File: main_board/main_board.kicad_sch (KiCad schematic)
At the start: 85 parts, among them J2 Conn_01x02, J3 Conn_01x02, J4 EncSide, J5 MainSide, J6 EncSide, J7 MainSide, Q1 ST-1KL3A, Q2 ST-1KL3A, Q3 ST-1KL3A, Q4 ST-1KL3A, Q5 IRLML6344, Q6 IRLML6344, Q7 IRLML6344, Q8 IRLML6344, U1 ADCS7476, U10 AS5047D, U11 LSM6DSR, U2 BD63573NUV, U3 ADCS7476, U4 ADCS7476, U5 BD63573NUV, U6 ESP32-S3-PICO-1-N8R2, U7 AS5047D, U8 ADCS7476, U9 ADCS7476

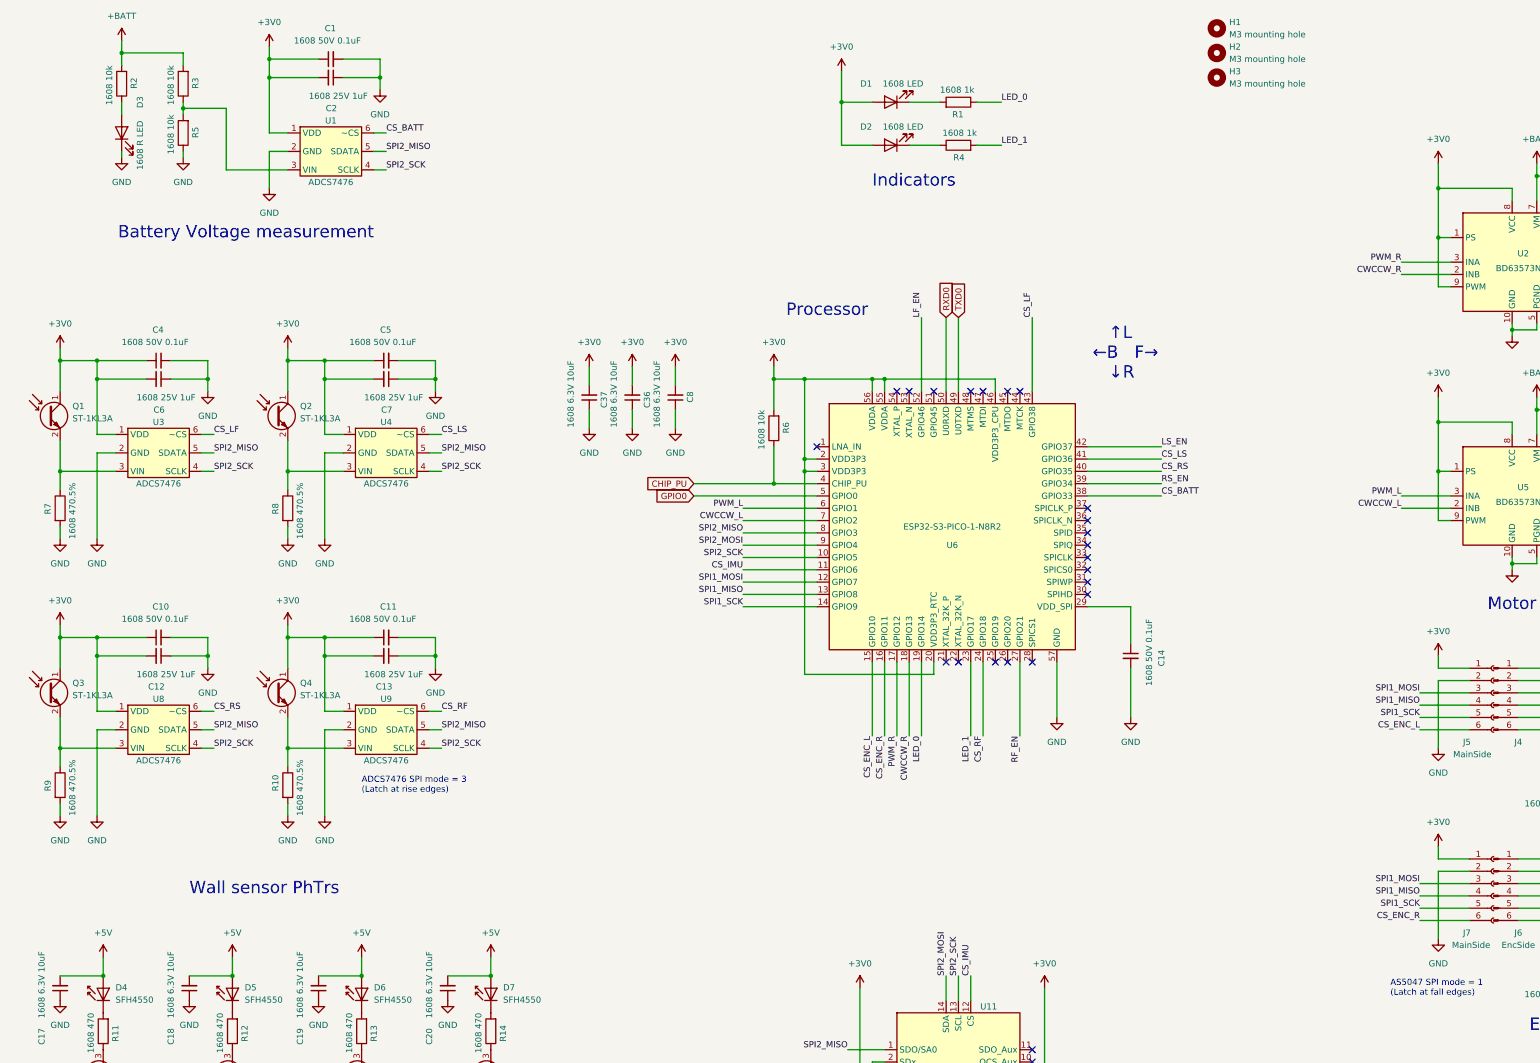
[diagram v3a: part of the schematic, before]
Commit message: 回路図 : 3.0Vから3.3Vに変更 アートワーク : コネクタピン配などのシルクを追加
Signed-off-by: Kazuki Iida <elkel53930@gmail.com>
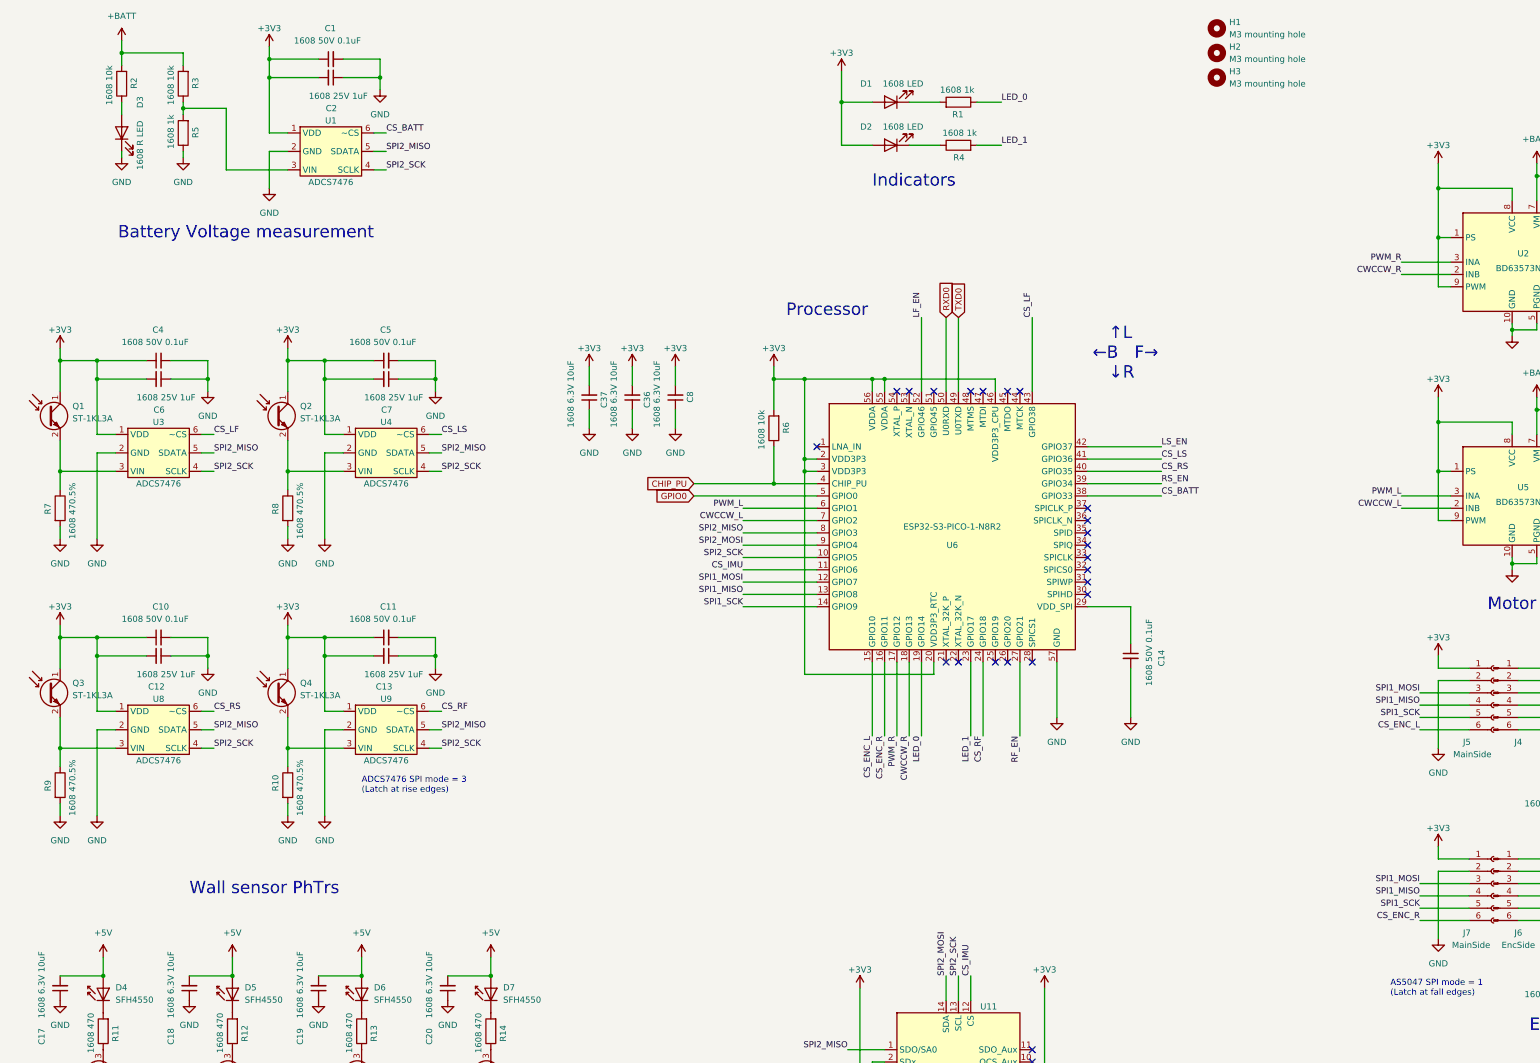
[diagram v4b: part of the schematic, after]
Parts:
- R5: value 1608 10k -> 1608 1k
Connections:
- net +3V0 renamed +3V3

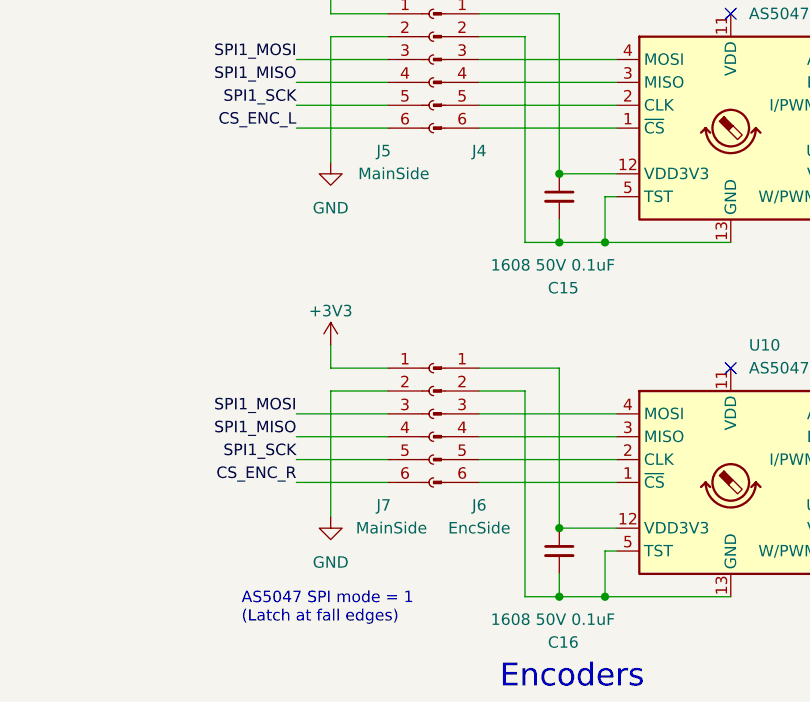
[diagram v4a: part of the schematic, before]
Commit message: 定数や型番の修正
Signed-off-by: Kazuki Iida <elkel53930@gmail.com>
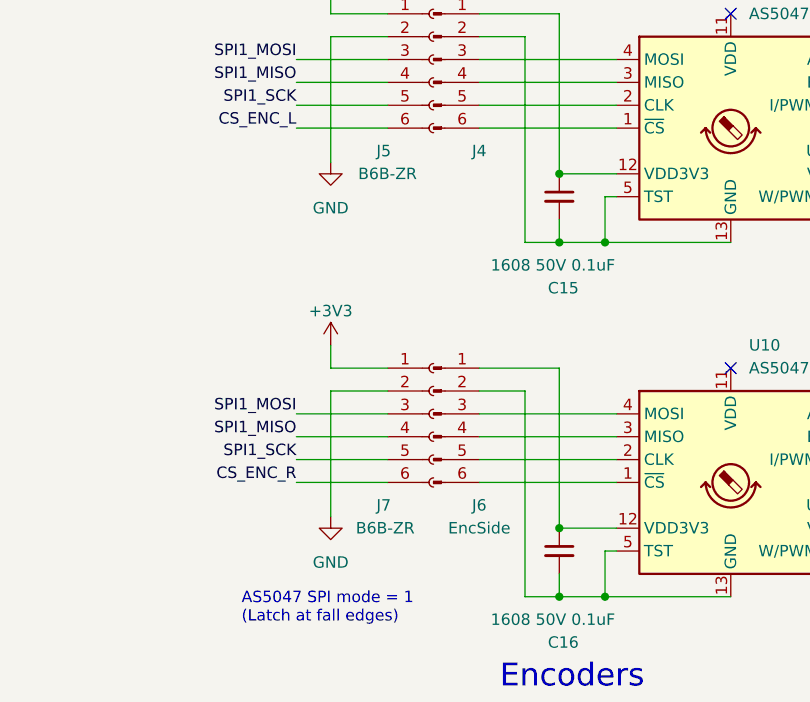
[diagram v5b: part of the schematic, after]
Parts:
- J5, J7: value MainSide -> B6B-ZR
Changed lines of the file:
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@@
 			)
 		)
-		(property "Value" "MainSide"
+		(property "Value" "B6B-ZR"
 			(at 325.374 213.36 0)
 			(effects
@@
 			)
 		)
-		(property "Value" "MainSide"
+		(property "Value" "B6B-ZR"
 			(at 325.628 173.99 0)
 			(effects

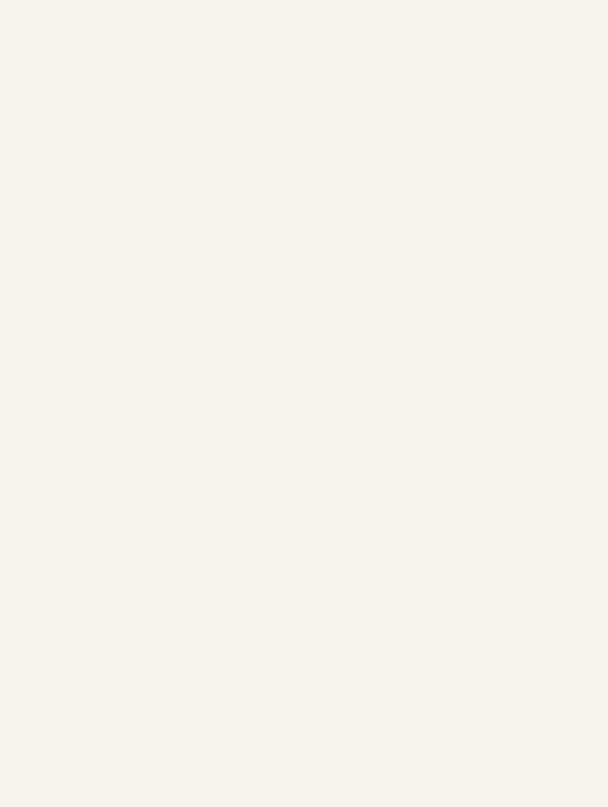
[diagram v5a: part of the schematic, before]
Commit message: 充電回路追加
Signed-off-by: Kazuki Iida <elkel53930@gmail.com>
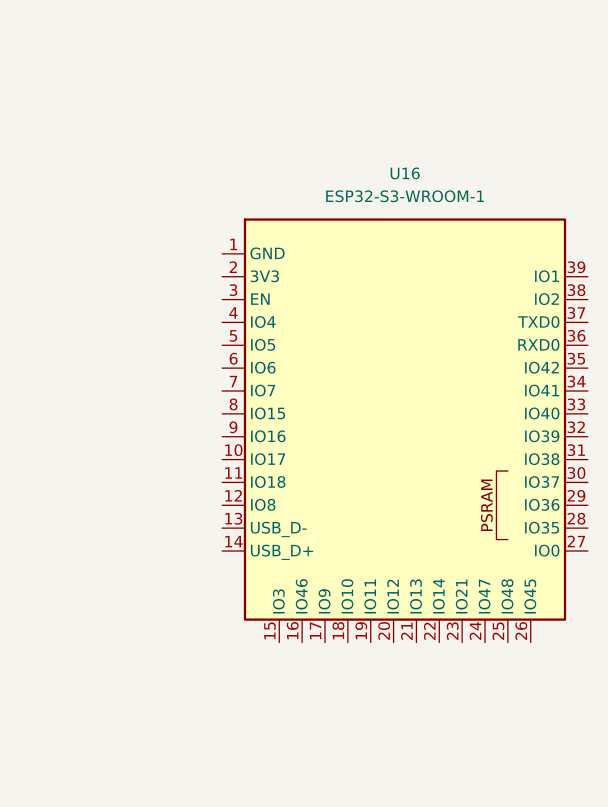
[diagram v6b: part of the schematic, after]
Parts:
- added U16: ESP32-S3-WROOM-1, RF_Module:ESP32-S3-WROOM-1, symbol micromouse-twilight:ESP32-S3-WROOM-1
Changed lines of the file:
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@@
+	)
+	(symbol
+		(lib_name "ESP32-S3-WROOM-1_1")
+		(lib_id "micromouse-twilight:ESP32-S3-WROOM-1")
+		(at 464.3719 167.5475 0)
+		(unit 1)
+		(exclude_from_sim no)
+		(in_bom yes)
+		(on_board yes)
+		(dnp no)
+		(fields_autoplaced yes)
+		(property "Reference" "U16"
+			(at 464.3719 140.8775 0)
+			(effects
+				(font
+					(size 1.27 1.27)
+				)
+			)
+		)
+		(property "Value" "ESP32-S3-WROOM-1"
+			(at 464.3719 143.4175 0)
+			(effects
+				(font
+					(size 1.27 1.27)
+				)
+			)
+		)
+		(property "Footprint" "RF_Module:ESP32-S3-WROOM-1"
+			(at 466.6579 133.0035 0)
+			(effects
+				(font
+					(size 1.27 1.27)
+				)
+				(hide yes)
+			)
+		)
+		(property "Datasheet" "https://www.espressif.com/sites/default/files/documentation/esp32-s3-wroom-1_wroom-1u_datasheet_en.pdf"
+			(at 465.1339 129.9555 0)
+			(effects
+				(font
+					(size 1.27 1.27)
+				)
+				(hide yes)
+			)
+		)
+		(property "Description" "RF Module, ESP32-S3 SoC, Wi-Fi 802.11b/g/n, Bluetooth, BLE, 32-bit, 3.3V, onboard antenna, SMD"
+			(at 464.3719 126.9075 0)
+			(effects
+				(font
+					(size 1.27 1.27)
+				)
+				(hide yes)
+			)
+		)
+		(pin "14"
+		)
+		(pin "13"
+		)
+		(pin "26"
+		)
+		(pin "22"
+		)
+		(pin "7"
+		)
+		(pin "6"
+		)
+		(pin "12"
+		)
+		(pin "10"
+		)
+		(pin "15"
+		)
+		(pin "9"
+		)
+		(pin "4"
+		)
+		(pin "1"
+		)
+		(pin "2"
+		)
+		(pin "8"
+		)
+		(pin "11"
+		)
+		(pin "18"
+		)
+		(pin "5"
+		)
+		(pin "3"
+		)
+		(pin "16"
+		)
+		(pin "21"
+		)
+		(pin "23"
+		)
+		(pin "24"
+		)
+		(pin "17"
+		)
+		(pin "19"
+		)
+		(pin "20"
+		)
+		(pin "25"
+		)
+		(pin "36"
+		)
+		(pin "29"
+		)
+		(pin "34"
+		)
+		(pin "35"
+		)
+		(pin "38"
+		)
+		(pin "30"
+		)
+		(pin "37"
+		)
+		(pin "31"
+		)
+		(pin "28"
+		)
+		(pin "40"
+		)
+		(pin "27"
+		)
+		(pin "33"
+		)
+		(pin "39"
+		)
+		(pin "41"
+		)
+		(pin "32"
+		)
+		(instances
+			(project "main_board"
+				(path "/d2cf6a41-8170-4aa9-b19e-2c9825cc9c77"
+					(reference "U16")
+					(unit 1)
+				)
+			)
+		)
 	)
 	(symbol

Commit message: 部品名追加
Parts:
- removed C36, C37: 1608 6.3V 10uF, Capacitor_SMD:C_0603_1608Metric, symbol Device:C_Small
- removed R6: 1608 10k, Resistor_SMD:R_0603_1608Metric, symbol Device:R
- removed U6: ESP32-S3-PICO-1-N8R2, Package_DFN_QFN:QFN-56-1EP_7x7mm_P0.4mm_EP4x4mm, symbol micromouse:ESP32-S3FN8
- C1, C10, C11, C14, C15, C16, C21, C22, C4, C5: value 1608 50V 0.1uF -> CC0603KRX7R9BB104
- C12, C13, C2, C6, C7: value 1608 25V 1uF -> CL10A105KB8NNNC
- C17, C18, C19, C20: value 1608 6.3V 10uF -> CL10A106KP8NNNC
- C3, C9: value 3225 3.3u 16V -> CL21A106KAYNNNE; footprint Capacitor_SMD:C_1210_3225Metric -> Capacitor_SMD:C_0805_2012Metric; フィールド4 16MU335KB33225 -> (none)
- C8: value 1608 6.3V 10uF -> CL21A106KAYNNNE; footprint Capacitor_SMD:C_0603_1608Metric -> Capacitor_SMD:C_0805_2012Metric
- D1: value 1608 LED -> D-060306G1/SS2/G1
- D2: value 1608 LED -> KT-0603R; フィールド4 (none) -> 1608 Red
- D3: value 1608 R LED -> D-060306G1/SS2/G1
- R1, R4, R5: value 1608 1k -> 0603WAF1001T5E
- R10, R7, R8, R9: value 1608 470.5% -> 0603WAF4700T5E
- R11, R12, R13, R14: value 1608 470 -> 0603WAF4700T5E
- R15, R16, R17, R18, R2, R3: value 1608 10k -> 0603WAF1002T5E
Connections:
- net +3V3: now also C14.2, C21.2, C22.2, U16.2 (3V3); no longer C21.1, C22.1
- net +BATT: now also C3.2, C9.2; no longer C3.1, C9.1
- net CHIP_PU: now also U16.3 (EN)
- net CS_BATT: now also U16.33 (IO40)
- net CS_ENC_L: now also U16.13 (USB_D-)
- net CS_ENC_R: now also U16.14 (USB_D+)
- net CS_IMU: now also U16.20 (IO12)
- net CS_LF: now also U16.4 (IO4)
- net CS_LS: now also U16.6 (IO6)
- net CS_RF: now also U16.39 (IO1)
- net CS_RS: now also U16.35 (IO42)
- net CWCCW_L: now also U16.16 (IO46)
- net CWCCW_R: now also U16.25 (IO48)
- net GND: now also C14.1, C21.1, C22.1, C3.1, C9.1, R10.1, R5.2, R7.1, R8.1, R9.1, U16.1 (GND); no longer C14.2, C21.2, C22.2, C3.2, C9.2, R10.2, R5.1, R7.2, R8.2, R9.2
- net GPIO0: now also U16.27 (IO0)
- net LED_0: now also U16.8 (IO15)
- net LED_1: now also R4.1, U16.9 (IO16); no longer R4.2
- net LF_EN: now also U16.5 (IO5)
- net LS_EN: now also U16.7 (IO7)
- net PWM_L: now also U16.15 (IO3)
- net PWM_R: now also U16.24 (IO47)
- net RF_EN: now also U16.38 (IO2)
- net RS_EN: now also U16.34 (IO41)
- net RXD0: now also U16.36 (RXD0)
- net SPI1_MISO: now also U16.11 (IO18)
- net SPI1_MOSI: now also U16.10 (IO17)
- net SPI1_SCK: now also U16.12 (IO8)
- net SPI2_MISO: now also U16.17 (IO9)
- net SPI2_MOSI: now also U16.18 (IO10)
- net SPI2_SCK: now also U16.19 (IO11)
- net TXD0: now also U16.37 (TXD0)
- net at R3.1, U1.3 (VIN): now also R5.1; no longer R5.2
- net at J4.1 (Pin_1), U7.12 (VDD3V3): now also C15.2; no longer C15.1
- net at J4.2 (Pin_2), U7.13 (GND), U7.5 (TST): now also C15.1; no longer C15.2
- net at Q4.2 (E), U9.3 (VIN): now also R10.2; no longer R10.1
- net at Q2.2 (E), U4.3 (VIN): now also R8.2; no longer R8.1
- net at Q1.2 (E), U3.3 (VIN): now also R7.2; no longer R7.1
- net at J6.1 (Pin_1), U10.12 (VDD3V3): now also C16.2; no longer C16.1
- net at J6.2 (Pin_2), U10.13 (GND), U10.5 (TST): now also C16.1; no longer C16.2
- net at D2.1 (K): now also R4.2; no longer R4.1
- net at Q3.2 (E), U8.3 (VIN): now also R9.2; no longer R9.1
- no-connect marks 39 -> 27
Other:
- note added: "↑ FRONT"
- note removed: "↑L ←B F→ ↓R"
- moved on the sheet: U16

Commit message: アートワーク開始
Signed-off-by: Kazuki Iida <elkel53930@gmail.com>
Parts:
- removed C18, C19: CL10A106KP8NNNC, Capacitor_SMD:C_0603_1608Metric, symbol Device:C_Small
- removed D4, D5: SFH4550, Library:SFH4550_Mirror, symbol LED:SFH4550
- removed D6, D7: SFH4550, Library:SFH4550, symbol LED:SFH4550
- removed Q1, Q2: ST-1KL3A, Library:ST-1KL3A_Mirror, symbol Device:Q_Photo_NPN
- removed Q3, Q4: ST-1KL3A, Library:ST-1KL3A, symbol Device:Q_Photo_NPN
- added H4: M2.6 mounting hole, Library:M2.6 Mounting Hole, symbol Mechanical:MountingHole
- added J3, J6: 2.54mm PinHeader, Connector_PinHeader_2.54mm:PinHeader_2x05_P2.54mm_Vertical, symbol Connector_Generic:Conn_02x05_Odd_Even
- H1, H2, H3: value M3 mounting hole -> M2.6 mounting hole; footprint MountingHole:MountingHole_3.2mm_M3 -> Library:M2.6 Mounting Hole
- renumbered C9 to C10, C10 to C11, C11 to C12, C12 to C13, C13 to C14, C14 to C8, C8 to C9, D3 to D1, D1 to D2, D2 to D3, H11 to H10, H4 to H5, H10 to H9, J2 to J1, J3 to J2, J6 to J7, J7 to J8, Q5 to Q1, Q6 to Q2, Q7 to Q3, Q8 to Q4, R2 to R1, R11 to R10, R12 to R11, R13 to R12, R14 to R13, R15 to R14, R16 to R15, R17 to R16, R18 to R17, R3 to R2, R5 to R3, R1 to R4, R4 to R5, R7 to R6, R8 to R7, R9 to R8, R10 to R9, U16 to U6, U8 to U7, U9 to U8, U7 to U9
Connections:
- net +3V3: now also C20.2, J3.10 (Pin_10), J3.7 (Pin_7), J3.8 (Pin_8), J3.9 (Pin_9)
- net +5V: now also J6.10 (Pin_10), J6.7 (Pin_7), J6.8 (Pin_8), J6.9 (Pin_9); no longer C20.2
- net LED_0: now also U6.4 (IO4); no longer U6.8 (IO15)
- net LED_1: now also U6.5 (IO5); no longer U6.9 (IO16)
- net LF_EN: now also U6.6 (IO6); no longer U6.5 (IO5)
- net RS_EN: now also U6.35 (IO42); no longer U6.34 (IO41)
- net RF_PHTR: now reaches R9.2, U8.3 (VIN)
- net RF_PHTR: now also J6.3 (Pin_3)
- net LS_PHTR: now reaches R7.2, U4.3 (VIN)
- net LS_PHTR: now also J3.2 (Pin_2)
- net RS_PHTR: now reaches R8.2, U7.3 (VIN)
- net RS_PHTR: now also J6.1 (Pin_1)
- net LF_PHTR: now reaches R6.2, U3.3 (VIN)
- net LF_PHTR: now also J3.4 (Pin_4)
- net LS_LED: now reaches R11.2
- net LS_LED: now also J3.1 (Pin_1)
- net RF_LED: now reaches R13.2
- net RF_LED: now also J6.4 (Pin_4)
- net LF_LED: now reaches R10.2
- net LF_LED: now also J3.3 (Pin_3)
- net RS_LED: now reaches R12.2
- net RS_LED: now also J6.2 (Pin_2)
- net CS_BATT renamed BATT_CS
- net BATT_CS: now also U6.39 (IO1); no longer U6.33 (IO40)
- net CS_LF renamed LF_CS
- net LF_CS: now also U6.9 (IO16); no longer U6.4 (IO4)
- net CS_LS renamed LS_CS
- net LS_CS: now also U6.8 (IO15); no longer U6.6 (IO6)
- net CS_RF renamed RF_CS
- net RF_CS: now also U6.33 (IO40); no longer U6.39 (IO1)
- net CS_RS renamed RS_CS
- net RS_CS: now also U6.34 (IO41); no longer U6.35 (IO42)
- no-connect marks 27 -> 31
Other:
- note added: "LEDs are mounted on the sub-board."
- note added: "PhTrs are mounted on the sub-board."
- note added: "Sensor sub board connector"
- moved on the sheet: C11, C12, C13, C14, C20, C21, C22, C4, C5, C6, C7, C8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
